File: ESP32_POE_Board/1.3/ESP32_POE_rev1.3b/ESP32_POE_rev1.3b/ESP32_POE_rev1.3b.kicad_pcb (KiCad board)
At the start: 4 copper layers, 28 x 80 mm, 161 parts, among them J1 RS1-02-G, J10 HMTSW-102-X-X-S-X, J11 HMTSW-102-X-X-S-X, J12 HMTSW-102-X-X-S-X, J13 RS1-02-G, J14 RS1-02-G, J15 RS1-02-G, J16 RS1-02-G, J17 RS1-02-G, J18 RS1-02-G, J19 RS1-02-G, J2 HMTSW-102-X-X-S-X, J20 HMTSW-102-X-X-S-X, J21 HMTSW-102-X-X-S-X, J22 HMTSW-102-X-X-S-X, J23 HMTSW-102-X-X-S-X, J24 HMTSW-102-X-X-S-X, J25 SI-46020-F, J26 USB_C_Receptacle, J3 RS1-02-G, J4 RS1-02-G, J5 RS1-02-G, J6 RS1-02-G, J7 HMTSW-102-X-X-S-X, J8 HMTSW-102-X-X-S-X, J9 HMTSW-102-X-X-S-X, Q1 Q12MHz/20pF/10ppm/4P/3.2x2.5mm, Q2 BC817-40(SOT23), Q3 BC817-40(SOT23), SW1 PTS815 SJM 250 SMTR LFS, SW2 PTS815 SJM 250 SMTR LFS, T1 LMUN2211LT1G(SOT-23), U1 CH340T(SSOP20W), U2 TPS2375D(SO-8), U3 BL4054B-42TPRN(SOT23-5), U4 LAN8710A-EZC(QFN32), U5 TX4138(ESOIC-8), U6 ESP32-WROVER-E, U7 SY8089AAAC(SOT23-5), U8 SN74LVC1G04DBVR(SOT23-5)

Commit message: updates
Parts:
- removed C20: 1uF/10V/20%/X5R/C0603, OLIMEX_RLC-FP:C_0603_5MIL_DWS
- removed C28, C8: 100nF/16V/10%/X7R/C0402, OLIMEX_RLC-FP:C_0402_5MIL_DWS
- removed C3: 47uF/6.3V/20%/X5R/C0805, OLIMEX_RLC-FP:C_0805_5MIL_DWS
- removed C4, C5: 27pF/50V/5%/C0G/C0402, OLIMEX_RLC-FP:C_0402_5MIL_DWS
- removed C7: 22uF/6.3V/20%/X5R/C0603, OLIMEX_RLC-FP:C_0603_5MIL_DWS
- removed D2: BAT54C(SOT23-3), OLIMEX_Diodes-FP:SOT23-3
- removed D4, D6, D7, D9: 1N5819S4(SOD-123), OLIMEX_Diodes-FP:SOD-123_1C-2A_KA
- removed H1, H2, H3, H4: MountingHole, MountingHole:MountingHole_2.1mm
- removed J10, J11, J12, J2, J20, J21, J22, J23, J24, J7, J8, J9: HMTSW-102-X-X-S-X, HMTSW-102-X-X-S-X:SAMTEC_HMTSW-102-X-X-S-X
- removed J26: USB_C_Receptacle, Connector_USB:USB_C_Receptacle_Molex_105450-0101-L
- removed L3, L5: FB0805/600R/2A, OLIMEX_RLC-FP:L_0805_5MIL_DWS
- removed LAN_CON1: RJP-003TC1(LPJ4112CNL), OLIMEX_Connectors-FP:RJP-003TC1(LPJ4112CNL)
- removed Q1: Q12MHz/20pF/10ppm/4P/3.2x2.5mm, OLIMEX_Crystal-FP:TSX-3.2x2.5mm_GND(3)
- removed Q2, Q3: BC817-40(SOT23), OLIMEX_Transistors-FP:SOT23
- removed R16: NA(10k/R0402), OLIMEX_RLC-FP:R_0402_5MIL_DWS
- removed R18, R19, R32, R36, R37, R39, R48: 10k/R0402, OLIMEX_RLC-FP:R_0402_5MIL_DWS
- removed R20, R21: 1k/R0402, OLIMEX_RLC-FP:R_0402_5MIL_DWS
- removed R24, R46, R47: 220R/R0402, OLIMEX_RLC-FP:R_0402_5MIL_DWS
- removed R31, R35: 2.2k/R0402, OLIMEX_RLC-FP:R_0402_5MIL_DWS
- removed R40, R45: 10R/R0402, OLIMEX_RLC-FP:R_0402_5MIL_DWS
- removed R44, R49: NA/R0402, OLIMEX_RLC-FP:R_0402_5MIL_DWS
- removed RM3: RA1206_(4X0603)_4B8_2.2k, OLIMEX_RLC-FP:R_MATRIX_4
- removed SW1, SW2: PTS815 SJM 250 SMTR LFS, PTS815:SW4_PTS815 SJM 250 SMTR LFS_CNK
- removed U1: CH340T(SSOP20W), OLIMEX_IC-FP:SSOP-20W
- removed U6: ESP32-WROVER-E, OLIMEX_Cases-FP:ESP32-WROVER(WROOM)-UNIVERSAL_MODULE
- removed U8: SN74LVC1G04DBVR(SOT23-5), OLIMEX_IC-FP:SOT-23-5
- removed UEXT1: P-B-V-10-LF, OLIMEX_Connectors-FP:GBH-254-SMT-10
- removed USB-UART1: MISB-SWMM-5B-LF(USB_MICRO), OLIMEX_Connectors-FP:USB-MICRO_MISB-SWMM-5B_LF
- moved J25 73.6 mm to (109.1, 170.4)
- moved J19 0.74 mm to (164.2, 101.7)
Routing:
- net (no net): track 0.00 -> 1302.6 mm, vias 0 -> 54
- net /GPIO1\U0TXD: track 99.3 -> 0.00 mm, vias 3 -> 0
- net /GPIO16\I2C-SCL: track 95.9 -> 0.00 mm, vias 4 -> 0
- net /GPIO3\U0RXD: track 95.6 -> 0.00 mm, vias 4 -> 0
- net /GPIO14\HS2_CLK: track 84.1 -> 0.00 mm, vias 2 -> 0
- net /GPIO2\HS2_DATA0: track 78.9 -> 0.00 mm, vias 3 -> 0
- net /GPIO5\SPI_CS: track 68.8 -> 0.00 mm, vias 4 -> 0
- net /GPIO0: track 67.8 -> 0.00 mm, vias 2 -> 0
- net /GPI34\BUT1: track 66.5 -> 0.00 mm, vias 4 -> 0
- net /D_Com: track 66.5 -> 0.00 mm, vias 3 -> 0
- net /GPIO4\U1TXD: track 66.0 -> 0.00 mm, vias 3 -> 0
- net /GPIO32: track 60.9 -> 0.00 mm, vias 2 -> 0
- net /GPIO13\I2C-SDA: track 59.5 -> 0.00 mm, vias 3 -> 0
- net /GPI36\U1RXD: track 58.2 -> 0.00 mm, vias 3 -> 0
- net /GPIO33: track 52.4 -> 0.00 mm, vias 2 -> 0
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
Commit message: board edges
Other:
- board size 28 x 80 mm -> 83.1 x 80 mm
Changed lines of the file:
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@@
     (fp_arc (start 5.399 -11.85) (mid 5.964756 -11.615656) (end 6.1991 -11.0499)
       (stroke (width 0.127) (type solid)) (layer "B.Fab"))
-    (fp_arc (start 5.497065 -5.78448) (mid 5.527682 -5.938445) (end 5.6149 -6.06896)
+    (fp_arc (start 5.497065 -5.78448) (mid 5.527688 -5.938439) (end 5.6149 -6.06896)
       (stroke (width 0.127) (type solid)) (layer "B.Fab"))
-    (fp_arc (start 5.69872 -4.7507) (mid 5.556805 -4.809462) (end 5.49806 -4.95136)
+    (fp_arc (start 5.69872 -4.7507) (mid 5.55684 -4.809469) (end 5.49806 -4.95136)
       (stroke (width 0.127) (type solid)) (layer "B.Fab"))
-    (fp_arc (start 6.0975 -4.75324) (mid 6.169356 -4.723484) (end 6.1991 -4.65164)
+    (fp_arc (start 6.0975 -4.75324) (mid 6.169321 -4.723478) (end 6.1991 -4.65164)
       (stroke (width 0.127) (type solid)) (layer "B.Fab"))
     (fp_arc (start 6.200095 -3.416498) (mid 6.169336 -3.262917) (end 6.08226 -3.13272)
@@
     (fp_arc (start 2.159 1.27) (mid 2.069197 1.232803) (end 2.032 1.143)
       (stroke (width 0.254) (type solid)) (layer "B.SilkS"))
-    (fp_arc (start 2.224065 2.284155) (mid 2.619864 2.433424) (end 2.921 2.7305)
+    (fp_arc (start 2.224065 2.284155) (mid 2.619862 2.433425) (end 2.921 2.7305)
       (stroke (width 0.254) (type solid)) (layer "B.SilkS"))
-    (fp_arc (start 2.224929 1.013456) (mid 2.269175 1.033812) (end 2.286 1.0795)
+    (fp_arc (start 2.224929 1.013456) (mid 2.269136 1.033818) (end 2.286 1.0795)
       (stroke (width 0.254) (type solid)) (layer "B.SilkS"))
     (fp_arc (start 2.286 1.2065) (mid 2.267401 1.251401) (end 2.2225 1.27)
@@
     (fp_arc (start 3.995725 1.967506) (mid 3.773966 1.911122) (end 3.556 1.8415)
       (stroke (width 0.254) (type solid)) (layer "B.SilkS"))
-    (fp_arc (start 4.130538 2.030424) (mid 4.584614 2.174466) (end 4.953 2.4765)
+    (fp_arc (start 4.130538 2.030424) (mid 4.584615 2.174465) (end 4.953 2.4765)
       (stroke (width 0.254) (type solid)) (layer "B.SilkS"))
     (fp_arc (start 5.461699 2.666526) (mid 5.184934 2.631521) (end 4.953 2.4765)
@@
     (pad "32" smd rect (at -2.45 -1.75 90) (size 0.8 0.25) (layers "B.Cu" "B.Paste" "B.Mask")
       (net 59 "Net-(U4-RBIAS)") (pinfunction "RBIAS") (pintype "input") (solder_mask_margin 0.0508) (solder_paste_margin -0.01))
-    (pad "33" thru_hole rect locked (at -1.3 -0.5 90) (size 0.4 0.4) (drill 0.3) (layers "*.Cu" "B.Mask")
+    (pad "33" thru_hole rect (at -1.3 -0.5 90) (size 0.4 0.4) (drill 0.3) (layers "*.Cu" "B.Mask")
       (net 2 "GND") (pinfunction "GND") (pintype "power_in") (zone_connect 2))
-    (pad "33" thru_hole rect locked (at -1.3 0.5 90) (size 0.4 0.4) (drill 0.3) (layers "*.Cu" "B.Mask")
+    (pad "33" thru_hole rect (at -1.3 0.5 90) (size 0.4 0.4) (drill 0.3) (layers "*.Cu" "B.Mask")
       (net 2 "GND") (pinfunction "GND") (pintype "power_in") (zone_connect 2))
-    (pad "33" thru_hole rect locked (at -0.5 -1.3 90) (size 0.4 0.4) (drill 0.3) (layers "*.Cu" "B.Mask")
+    (pad "33" thru_hole rect (at -0.5 -1.3 90) (size 0.4 0.4) (drill 0.3) (layers "*.Cu" "B.Mask")
       (net 2 "GND") (pinfunction "GND") (pintype "power_in") (zone_connect 2))
-    (pad "33" thru_hole rect locked (at -0.5 1.3 90) (size 0.4 0.4) (drill 0.3) (layers "*.Cu" "B.Mask")
+    (pad "33" thru_hole rect (at -0.5 1.3 90) (size 0.4 0.4) (drill 0.3) (layers "*.Cu" "B.Mask")
       (net 2 "GND") (pinfunction "GND") (pintype "power_in") (zone_connect 2))
-    (pad "33" thru_hole rect locked (at 0 0 90) (size 1.4224 1.4224) (drill 1.2) (layers "*.Cu" "*.Mask")
+    (pad "33" thru_hole rect (at 0 0 90) (size 1.4224 1.4224) (drill 1.2) (layers "*.Cu" "*.Mask")
       (net 2 "GND") (pinfunction "GND") (pintype "power_in") (zone_connect 2))
     (pad "33" smd rect (at 0 0 90) (size 3.6 3.6) (layers "B.Cu" "B.Mask")
       (net 2 "GND") (pinfunction "GND") (pintype "power_in") (solder_mask_margin 0.0508))
-    (pad "33" thru_hole rect locked (at 0.5 -1.3 90) (size 0.4 0.4) (drill 0.3) (layers "*.Cu" "B.Mask")
+    (pad "33" thru_hole rect (at 0.5 -1.3 90) (size 0.4 0.4) (drill 0.3) (layers "*.Cu" "B.Mask")
       (net 2 "GND") (pinfunction "GND") (pintype "power_in") (zone_connect 2))
-    (pad "33" thru_hole rect locked (at 0.5 1.3 90) (size 0.4 0.4) (drill 0.3) (layers "*.Cu" "B.Mask")
+    (pad "33" thru_hole rect (at 0.5 1.3 90) (size 0.4 0.4) (drill 0.3) (layers "*.Cu" "B.Mask")
       (net 2 "GND") (pinfunction "GND") (pintype "power_in") (zone_connect 2))
-    (pad "33" thru_hole rect locked (at 1.3 -0.5 90) (size 0.4 0.4) (drill 0.3) (layers "*.Cu" "B.Mask")
+    (pad "33" thru_hole rect (at 1.3 -0.5 90) (size 0.4 0.4) (drill 0.3) (layers "*.Cu" "B.Mask")
       (net 2 "GND") (pinfunction "GND") (pintype "power_in") (zone_connect 2))
-    (pad "33" thru_hole rect locked (at 1.3 0.5 90) (size 0.4 0.4) (drill 0.29972) (layers "*.Cu" "B.Mask")
+    (pad "33" thru_hole rect (at 1.3 0.5 90) (size 0.4 0.4) (drill 0.29972) (layers "*.Cu" "B.Mask")
       (net 2 "GND") (pinfunction "GND") (pintype "power_in") (zone_connect 2))
     (model "${KIPRJMOD}/3d/QFN32_5x5.step"
@@
   (gr_line (start 90.15 90.15) (end 118.15 90.15)
     (stroke (width 0.254) (type solid)) (layer "Edge.Cuts"))
+  (gr_circle (center 153.2128 127.0508) (end 173.2128 127.0508)
+    (stroke (width 0.05) (type default)) (fill none) (layer "Edge.Cuts"))
   (gr_line (start 90.15 163.83) (end 90.15 170.15)
     (stroke (width 0.254) (type solid)) (layer "Edge.Cuts"))

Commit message: POE 2 board
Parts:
- removed Logo_OSHW: , OLIMEX_LOGOs-FP:LOGO_OPENHARDWARE_8x8
- removed Logo_Olimex: , OLIMEX_LOGOs-FP:OLIMEX_LOGO_TB
- removed MICRO_SD1: TFC-9P-1.7H(ATFFS150A01BR016), OLIMEX_Connectors-FP:uSD(TFC-9P-1.xH(ATFFS150A01BR016))
- removed Sign_Antistatic: Val**, OLIMEX_LOGOs-FP:LOGO_ANTISTATIC_1
- removed Sign_PB-Free: , OLIMEX_LOGOs-FP:LOGO_PBFREE
- removed Sign_RecycleBin: , OLIMEX_LOGOs-FP:LOGO_RECYCLEBIN_1
- added J2: HMTSW-102-X-X-S-X, HMTSW-102-X-X-S-X:SAMTEC_HMTSW-102-X-X-S-X, F.Cu at (129.7, 122.8)
- C26, D8, R22, R23, R27, R28, R43, R7, RM2, T1, U3: moved to F.Cu
- moved U5 88.1 mm to (87.7, 47.6)
- moved C18 84.7 mm to (22.9, 132.2)
- moved C17 81.2 mm to (27.4, 126.7)
- moved C9 80.1 mm to (24.8, 144.9)
- moved R7 78.1 mm to (78.4, 43.0), turned to 0 degrees
- moved R29 77.2 mm to (22.3, 168.0)
- moved L2 77.2 mm to (30.9, 170.2)
- moved C16 76.4 mm to (70.6, 219.9)
- moved R26 76.4 mm to (74.3, 220.3)
- moved R30 76.4 mm to (66.5, 222.2)
- moved TVS1 76.4 mm to (73.9, 222.8)
- moved TVS3 76.4 mm to (77.4, 222.9)
- moved C26 75.4 mm to (79.3, 71.4), turned to 180 degrees
- moved J1 74.0 mm to (102.0, 27.4)
- moved J13 74.0 mm to (111.4, 32.5)
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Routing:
- net (no net): track 1302.6 -> 0.00 mm, vias 54 -> 0
- net GND: track 380.7 -> 0.00 mm, vias 58 -> 0
- net /GPI35: track 139.7 -> 0.00 mm, vias 5 -> 0
- net +3.3V: track 100.8 -> 0.00 mm, vias 12 -> 0
- net +5V: track 91.6 -> 0.00 mm, vias 4 -> 0
- net +3.3VLAN: track 91.3 -> 0.00 mm, vias 4 -> 0
- net Spare1: track 84.1 -> 0.00 mm, vias 2 -> 0
- net /GPIO22\EMAC_TXD1(RMII): track 84.1 -> 0.00 mm, vias 2 -> 0
- net /GPIO19\EMAC_TXD0(RMII): track 83.9 -> 0.00 mm, vias 3 -> 0
- net Spare2: track 83.3 -> 0.00 mm, vias 4 -> 0
- net /GPIO21\EMAC_TX_EN(RMII): track 82.2 -> 0.00 mm, vias 3 -> 0
- net /GPIO23\MDC(RMII): track 78.7 -> 0.00 mm, vias 2 -> 0
- net /GPIO17\EMAC_CLK_OUT_180: track 74.9 -> 0.00 mm, vias 3 -> 0
- net /GPIO15\HS2_CMD: track 73.1 -> 0.00 mm, vias 3 -> 0
- net Net-(C2-Pad2): track 70.5 -> 0.00 mm, vias 13 -> 0
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- removed copper zone on In2.Cu, net +3.3V
- removed copper zone on B.Cu, net GND
- removed copper zone on F.Cu, net GND
- removed copper zone on In1.Cu, net GND
- removed copper zone on B.Cu, net Net-(C2-Pad2)
- removed copper zone on F.Cu, net Net-(C2-Pad2)
- removed copper zone on In1.Cu, net Net-(C2-Pad2)
- removed copper zone on In2.Cu, net Net-(C2-Pad2)
- removed copper zone on F.Cu, net Net-(D5-K)
- removed copper zone on B.Cu, net Net-(R28-Pad1)
- removed copper zone on In1.Cu, net Net-(R28-Pad1)
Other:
- board size 83.1 x 80 mm -> 40 x 40 mm
- board text removed: "(C) 2022"
- board text removed: "+"
- board text removed: "+3V3"
- board text removed: "+5V"
- board text removed: "-"
- board text removed: "1"
- board text removed: "2"
- board text removed: "3"
- board text removed: "4"
- board text removed: "Compliant"
- board text removed: "ESP32-PoE"
- board text removed: "ESP_EN"
- board text removed: "GND"
- board text removed: "GPI34"
- board text removed: "GPI35"
- board text removed: "GPI36"
- board text removed: "GPI39"
- board text removed: "GPIO0"
- board text removed: "GPIO1"
- board text removed: "GPIO13"
- board text removed: "GPIO14"
- board text removed: "GPIO15"
- board text removed: "GPIO16"
- board text removed: "GPIO2"
- board text removed: "GPIO3"
- board text removed: "GPIO32"
- board text removed: "GPIO33"
- board text removed: "GPIO4"
- board text removed: "GPIO5"
- board text removed: "Rev.L"
- board text removed: "RoHS"
- board text removed: "www.olimex.com"

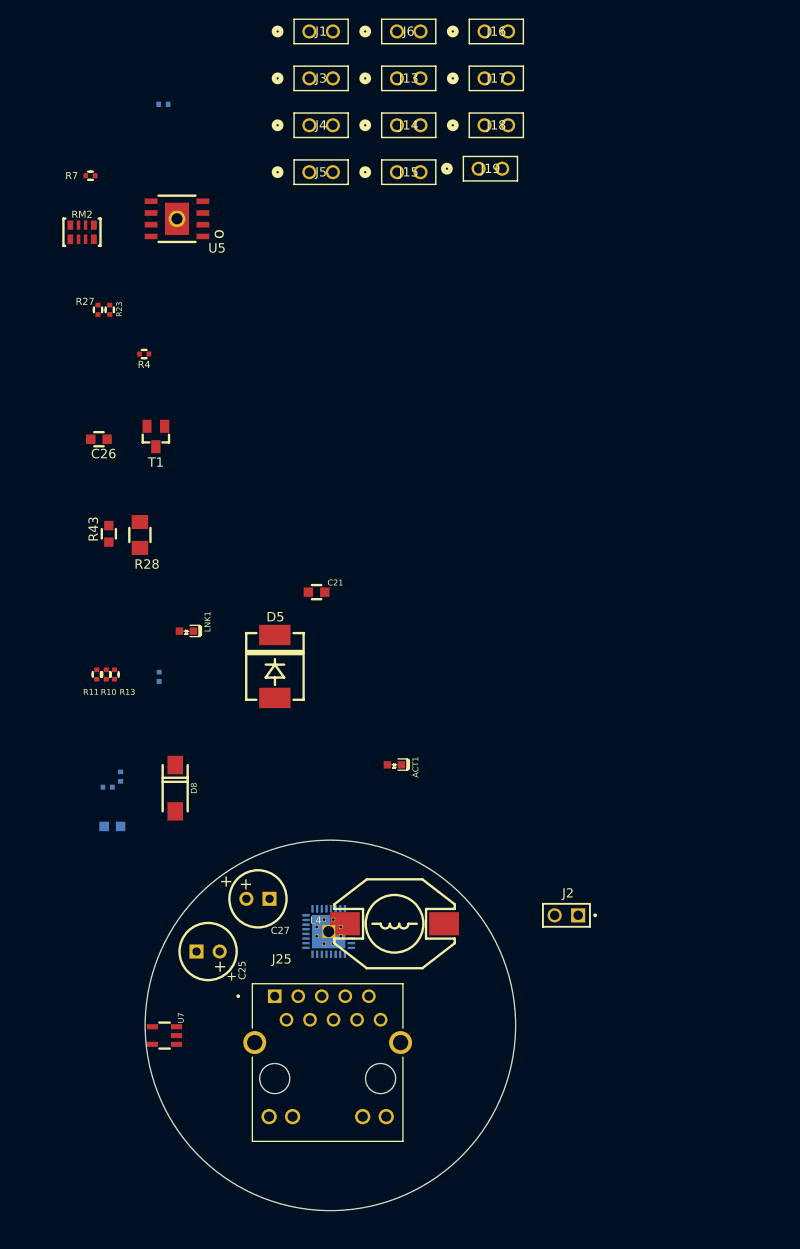
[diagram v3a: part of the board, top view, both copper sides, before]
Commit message: updated power
finished swapping power board bulk cap, new POE board schematic
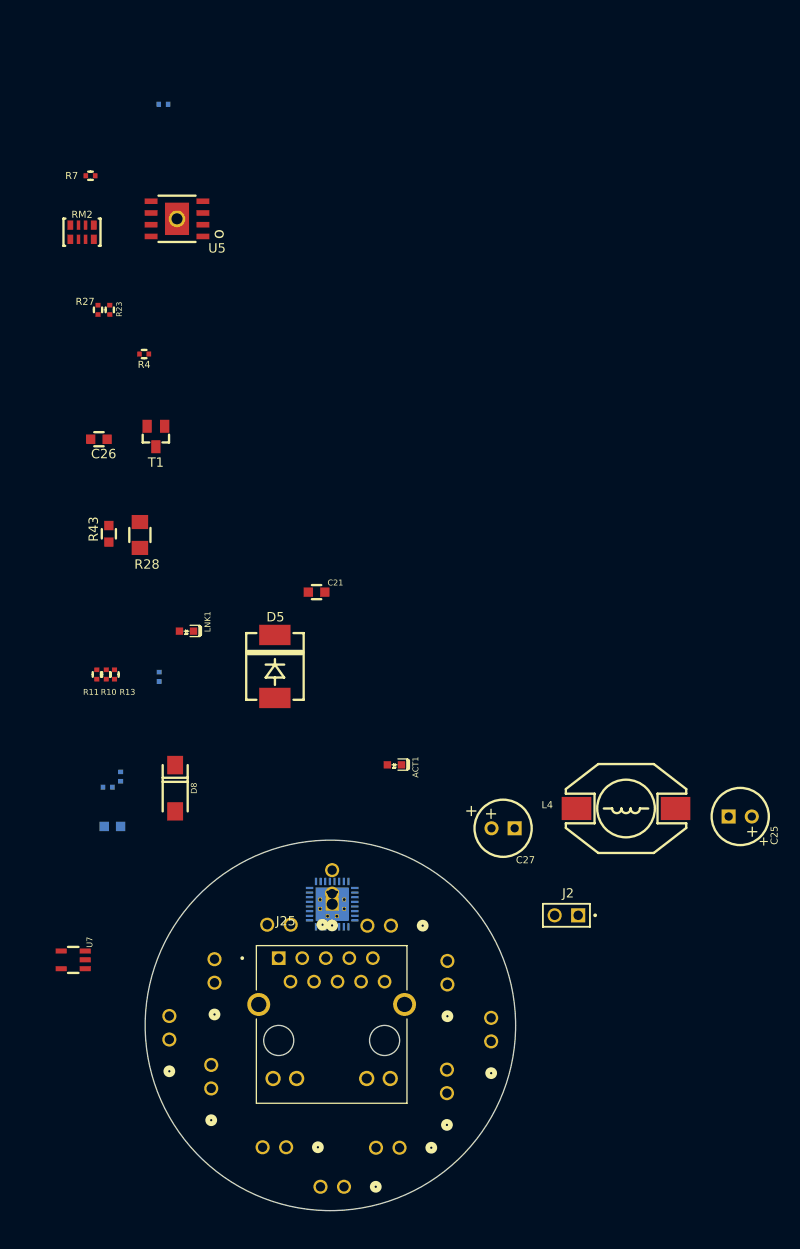
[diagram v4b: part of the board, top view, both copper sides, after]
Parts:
- J1, J13, J14, J15, J16, J17, J18, J19, J3, J4, J5, J6: moved to B.Cu
- moved J13 119.8 mm to (105.7, 152.1), turned to 180 degrees
- moved J17 115.8 mm to (111.7, 147.9), turned to 180 degrees
- moved J1 115.6 mm to (116.8, 142.0), turned to 90 degrees
- moved J3 115.4 mm to (99.5, 147.9), turned to 180 degrees
- moved J6 109.5 mm to (121.6, 136.4), turned to 90 degrees
- moved J18 108.1 mm to (91.4, 141.5), turned to 90 degrees
- moved J16 103.0 mm to (116.9, 130.3), turned to 90 degrees
- moved J4 99.9 mm to (86.9, 136.2), turned to 90 degrees
- moved J14 94.7 mm to (91.7, 130.1), turned to 90 degrees
- moved J19 84.1 mm to (100.0, 123.9), turned to 180 degrees
- moved J15 81.4 mm to (110.8, 124.0), turned to 180 degrees
- moved J5 77.9 mm to (104.4, 120.5), turned to 90 degrees
- moved C25 59.3 mm to (148.5, 112.2)
- moved L4 27.9 mm to (136.2, 111.3)
- moved C27 27.5 mm to (122.9, 113.4)
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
